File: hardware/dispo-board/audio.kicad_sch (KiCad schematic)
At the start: 41 parts, among them U3 OPA1671, U4 CS5343-CZZ, U5 OPA1671, U6 CS4344-CZZR

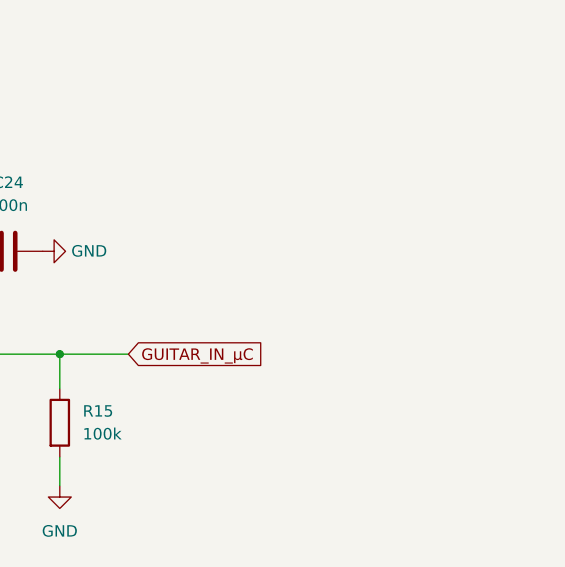
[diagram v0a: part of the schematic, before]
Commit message: basic software, bandpass fir filter, added notes to hardware modifications
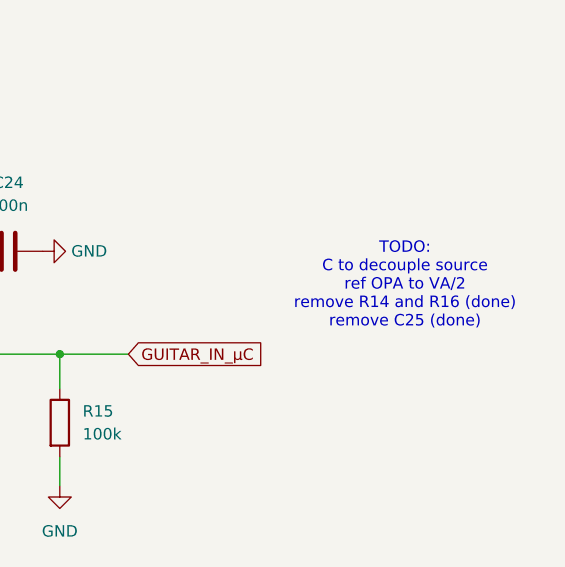
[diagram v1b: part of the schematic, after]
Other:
- note added: "TODO: C to decouple source ref OPA to VA/2 remove R14 and R16 (done) remove C25 (done)"
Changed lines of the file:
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@@
+		)
+	)
+	(text "TODO:\nC to decouple source\nref OPA to VA/2\nremove R14 and R16 (done)\nremove C25 (done)"
+		(exclude_from_sim no)
+		(at 230.124 43.18 0)
+		(effects
+			(font
+				(size 1.27 1.27)
+			)
 		)
 	)

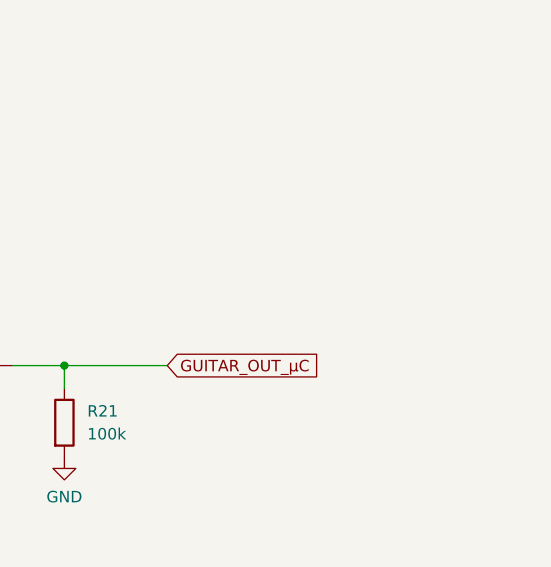
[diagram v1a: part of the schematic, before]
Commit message: audio nucleo changes, kicad notes for hardware issues
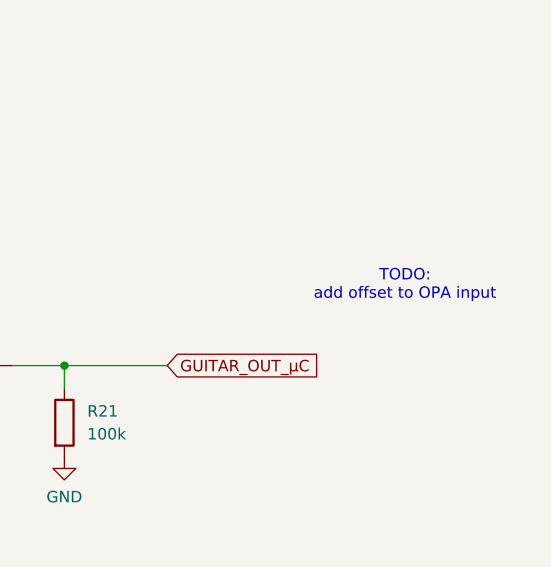
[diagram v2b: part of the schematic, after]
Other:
- note added: "TODO: add offset to OPA input"
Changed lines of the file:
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@@
+		)
+	)
+	(text "TODO:\nadd offset to OPA input"
+		(exclude_from_sim no)
+		(at 241.046 123.19 0)
+		(effects
+			(font
+				(size 1.27 1.27)
+			)
 		)
 	)

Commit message: abgabe version
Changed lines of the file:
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@@
 	(text "TODO:\nC to decouple source\nref OPA to VA/2\nremove R14 and R16 (done)\nremove C25 (done)"
 		(exclude_from_sim no)
-		(at 230.124 43.18 0)
+		(at 316.992 46.99 0)
 		(effects
 			(font
@@
 	(text "TODO:\nadd offset to OPA input"
 		(exclude_from_sim no)
-		(at 241.046 123.19 0)
+		(at 315.468 124.968 0)
 		(effects
 			(font

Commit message: schematic should be ready, changed parts, ...
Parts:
- removed C24, C30, C35: 100n, Capacitor_SMD:C_0402_1005Metric, symbol Device:C
- removed C31: 3u3, Capacitor_SMD:C_0603_1608Metric, symbol Device:C
- removed C33: 10n, Capacitor_SMD:C_0402_1005Metric, symbol Device:C
- removed C36: 10u, Capacitor_SMD:C_0603_1608Metric, symbol Device:C
- removed R19: 10k, Resistor_SMD:R_0402_1005Metric, symbol Device:R
- removed TP5: TestPoint, TestPoint:TestPoint_Pad_D1.5mm, symbol Connector:TestPoint
- removed U6: CS4344-CZZR, Package_SO:TSSOP-10_3x3mm_P0.5mm, symbol Audio:CS4344
- added C14: 10u, Capacitor_SMD:C_0603_1608Metric, symbol Device:C
- added C41: 10n, Capacitor_SMD:C_0402_1005Metric, symbol Device:C
- added C5, C6, C8: 100n, Capacitor_SMD:C_0402_1005Metric, symbol Device:C
- added U2: CS4344, Package_SO:TSSOP-10_3x3mm_P0.5mm, symbol Audio:CS4344
- C25, C32: value 1u -> 100n; footprint Capacitor_SMD:C_1206_3216Metric -> Capacitor_SMD:C_1210_3225Metric; MOUSER_NR 598-FCA1206A105M-H3 -> 667-ECH-U1C104JX5
- C26: MOUSER_NR 81-GRM1555C1H181JA1J -> 81-GCM1555C1H181JA6D
- C27, C29, C34: MOUSER_NR 81-GRM188C81A106MA3D -> 963-LMK107BBJ106MALT
- C28: MOUSER_NR 81-GRM15R61A104KA01J -> 963-MCASL105SB7104KF
- R13, R16: MOUSER_NR 71-CRCW040210K0FKEDC -> 652-CR0402-JW-103GLF
- R14: value 1k -> 10k; MOUSER_NR 71-CRCW0402-1.0K-E3 -> 71-CRCW040210K0FKEDC; now not fitted; now left out of the parts list
- R15, R21: footprint Resistor_SMD:R_0603_1608Metric -> Resistor_SMD:R_0402_1005Metric; MOUSER_NR 594-MCT0603MG1003BP5 -> 652-CR0402JW-104GLF
- R18: MOUSER_NR 667-ERA-2VEB4700X -> 667-ERA-2VEB4700X
- R22: now not fitted; now left out of the parts list
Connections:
- net +3.3VA: no longer U4.10 (VA)
- net GND: now also C14.2, C41.2, C5.2, C6.2, C8.2, U2.8 (GND)
- net GUITAR_IN_µC: now also C25.2; no longer R15.1, U3.3 (+)
- net I2S6_CK: now also U2.2 (~{DEM}/SCLK)
- net I2S6_MCK: now also U2.4 (MCLK)
- net I2S6_SDO: now also U2.1 (SDIN)
- net I2S6_WS: now also U2.3 (LRCK)
- net at R18.1: now also R14.2, R16.1, TP10.1, U2.10 (AOUTR), U2.7 (AOUTL)
- net at C34.1: now also U2.6 (FILT+)
- net at C26.1, TP4.1, U4.6 (AINL)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: now also RV1.1, U3.1 (OUT); no longer C25.1
- net at C28.1, U4.7 (VQ): now also C14.1; no longer C29.1
- net at R17.2, U5.5 (V+): now also R14.1, C6.1
- net at R12.2, U3.5 (V+): now also C5.1
- net at R18.2, TP11.1, U5.3 (+): now also C41.1
- new net: C25.1, R15.1, U3.3 (+)
- new net: C29.1, C8.1, U2.5 (VQ)
- new net +5VA: U2.9 (VA), U4.10 (VA)
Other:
- note added: "TODO: C to decouple source (done) ref OPA to VA/2 (cs5343 input_max = 0.5 va) remove R14 and R16 (done) remove C25 (done)"
- note added: "TODO: add offset to OPA input and output (propably not required)"
- note removed: "TODO: C to decouple source ref OPA to VA/2 remove R14 and R16 (done) remove C25 (done)"
- note removed: "TODO: add offset to OPA input"
- moved on the sheet: C26, R17, R18, RV1, RV2, TP1, TP10, TP11, TP2, TP3, TP6, TP7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

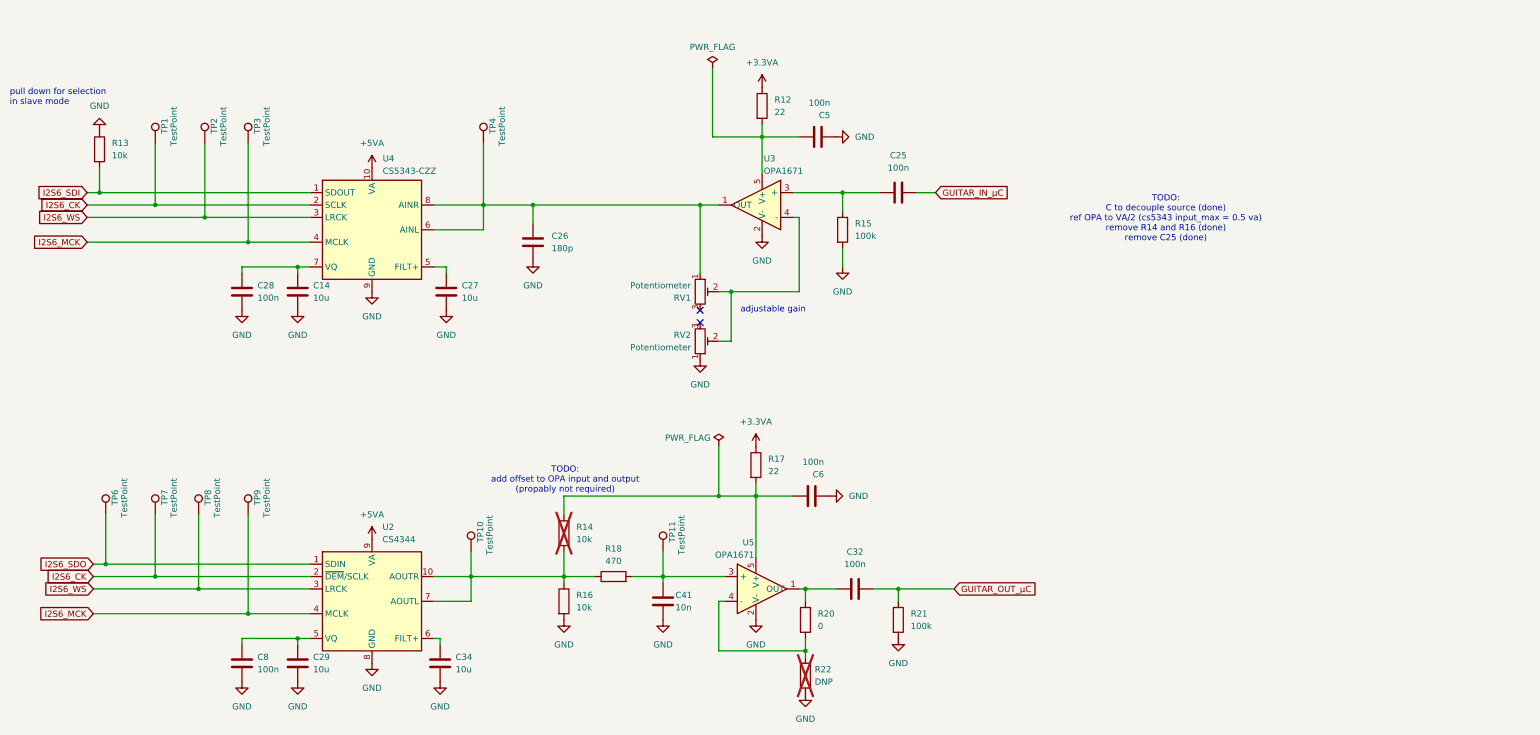
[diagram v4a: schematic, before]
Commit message: deleted nucleo board files, schematic ready?, changed to usb c
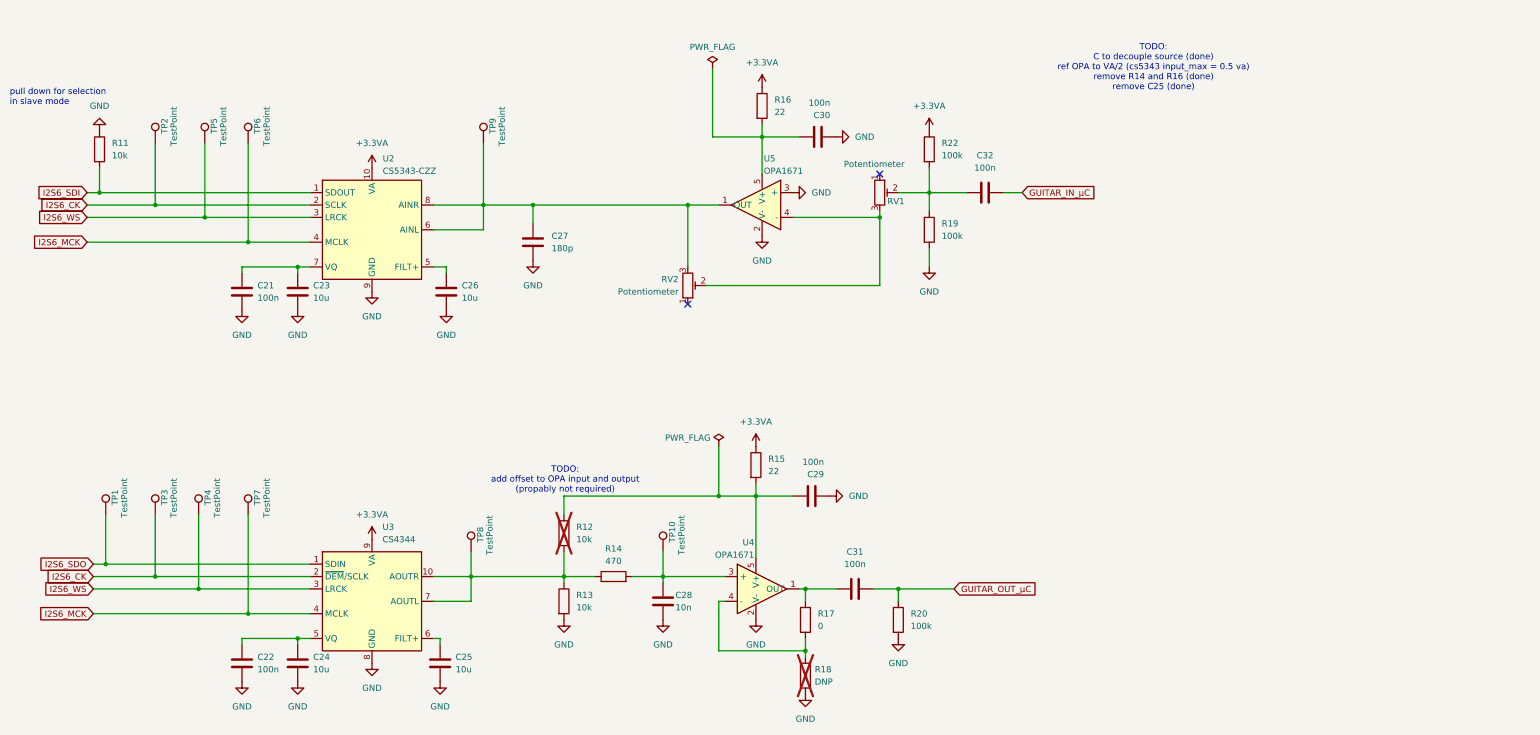
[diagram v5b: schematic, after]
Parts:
- added R22: 100k, Resistor_SMD:R_0402_1005Metric, symbol Device:R
- renumbered C28 to C21, C8 to C22, C14 to C23, C29 to C24, C34 to C25, C27 to C26, C26 to C27, C41 to C28, C6 to C29, C5 to C30, C32 to C31, C25 to C32, R13 to R11, R14 to R12, R16 to R13, R18 to R14, R17 to R15, R12 to R16, R20 to R17, R22 to R18, R15 to R19, R21 to R20, TP6 to TP1, TP11 to TP10, TP1 to TP2, TP7 to TP3, TP8 to TP4, TP2 to TP5, TP3 to TP6, TP9 to TP7, TP10 to TP8, TP4 to TP9, U4 to U2, U2 to U3, U5 to U4, U3 to U5
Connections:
- net +5VA is gone; now on net +3.3VA: U2.10 (VA), U3.9 (VA)
- net +3.3VA: now also R22.1
- net GND: now also U5.3 (+); no longer RV2.1
- net at C32.1, R19.1: now also RV1.2, R22.2; no longer U5.3 (+)
- net at RV2.2, U5.4 (-): now also RV1.3; no longer RV1.2
- net at RV2.3: now also C27.1, TP9.1, U2.6 (AINL), U2.8 (AINR), U5.1 (OUT)
- now unconnected: RV1.1
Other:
- note removed: "adjustable gain"
- moved on the sheet: C32, R19, RV1, RV2

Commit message: annotate schmetic
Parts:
- renumbered R20 to R19, R22 to R20, R19 to R21, RV2 to RV1, RV1 to RV2
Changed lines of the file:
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@@
 		(dnp no)
 		(fields_autoplaced yes)
-		(property "Reference" "#PWR053"
+		(property "Reference" "#PWR054"
 			(at 80.01 81.28 0)
 			(effects
@@
 			(project "dispo-board"
 				(path "/93ea4da8-8485-4fb5-a89d-c72021d94c09/9fac87bb-1399-44df-bfcb-579232522de8"
-					(reference "#PWR053")
+					(reference "#PWR054")
 					(unit 1)
 				)
@@
 		(dnp no)
 		(fields_autoplaced yes)
-		(property "Reference" "#PWR054"
+		(property "Reference" "#PWR055"
 			(at 80.01 157.48 0)
 			(effects
@@
 			(project "dispo-board"
 				(path "/93ea4da8-8485-4fb5-a89d-c72021d94c09/9fac87bb-1399-44df-bfcb-579232522de8"
-					(reference "#PWR054")
+					(reference "#PWR055")
 					(unit 1)
 				)
@@
 		(dnp no)
 		(fields_autoplaced yes)
-		(property "Reference" "R19"
+		(property "Reference" "R21"
 			(at 212.09 57.15 0)
 			(effects
@@
 			(project "dispo-board"
 				(path "/93ea4da8-8485-4fb5-a89d-c72021d94c09/9fac87bb-1399-44df-bfcb-579232522de8"
-					(reference "R19")
+					(reference "R21")
 					(unit 1)
 				)
@@
 		(dnp no)
 		(fields_autoplaced yes)
-		(property "Reference" "#PWR063"
+		(property "Reference" "#PWR064"
 			(at 154.94 144.78 0)
 			(effects
@@
 			(project "dispo-board"
 				(path "/93ea4da8-8485-4fb5-a89d-c72021d94c09/9fac87bb-1399-44df-bfcb-579232522de8"
-					(reference "#PWR063")
+					(reference "#PWR064")
 					(unit 1)
 				)
@@
 		(on_board yes)
 		(dnp no)
-		(property "Reference" "RV2"
+		(property "Reference" "RV1"
 			(at 158.115 68.58 0)
 			(effects
@@
 			(project "dispo-board"
 				(path "/93ea4da8-8485-4fb5-a89d-c72021d94c09/9fac87bb-1399-44df-bfcb-579232522de8"
-					(reference "RV2")
+					(reference "RV1")
 					(unit 1)
 				)
@@
 		(dnp no)
 		(fields_autoplaced yes)
-		(property "Reference" "#PWR052"
+		(property "Reference" "#PWR053"
 			(at 68.58 157.48 0)
 			(effects
@@
 			(project "dispo-board"
 				(path "/93ea4da8-8485-4fb5-a89d-c72021d94c09/9fac87bb-1399-44df-bfcb-579232522de8"
-					(reference "#PWR052")
+					(reference "#PWR053")
 					(unit 1)
 				)
@@
 		(dnp no)
 		(fields_autoplaced yes)
-		(property "Reference" "#PWR056"
+		(property "Reference" "#PWR057"
 			(at 95.25 77.47 0)
 			(effects
@@
 			(project "dispo-board"
 				(path "/93ea4da8-8485-4fb5-a89d-c72021d94c09/9fac87bb-1399-44df-bfcb-579232522de8"
-					(reference "#PWR056")
+					(reference "#PWR057")
 					(unit 1)
 				)
@@
 		(dnp no)
 		(fields_autoplaced yes)
-		(property "Reference" "R20"
+		(property "Reference" "R19"
 			(at 205.74 137.16 0)
 			(effects
@@
 			(project "dispo-board"
 				(path "/93ea4da8-8485-4fb5-a89d-c72021d94c09/9fac87bb-1399-44df-bfcb-579232522de8"
-					(reference "R20")
+					(reference "R19")
 					(unit 1)
 				)
@@
 		(dnp no)
 		(fields_autoplaced yes)
-		(property "Reference" "#PWR064"
+		(property "Reference" "#PWR069"
 			(at 187.96 50.8 0)
 			(effects
@@
 			(project ""
 				(path "/93ea4da8-8485-4fb5-a89d-c72021d94c09/9fac87bb-1399-44df-bfcb-579232522de8"
-					(reference "#PWR064")
+					(reference "#PWR069")
 					(unit 1)
 				)
@@
 		(dnp no)
 		(fields_autoplaced yes)
-		(property "Reference" "#PWR051"
+		(property "Reference" "#PWR052"
 			(at 68.58 81.28 0)
 			(effects
@@
 			(project ""
 				(path "/93ea4da8-8485-4fb5-a89d-c72021d94c09/9fac87bb-1399-44df-bfcb-579232522de8"
-					(reference "#PWR051")
+					(reference "#PWR052")
 					(unit 1)
 				)
@@
 		(dnp no)
 		(fields_autoplaced yes)
-		(property "Reference" "#PWR070"
+		(property "Reference" "#PWR071"
 			(at 195.58 113.03 0)
 			(effects
@@
 			(project "dispo-board"
 				(path "/93ea4da8-8485-4fb5-a89d-c72021d94c09/9fac87bb-1399-44df-bfcb-579232522de8"
-					(reference "#PWR070")
+					(reference "#PWR071")
 					(unit 1)
 				)
@@
 		(dnp no)
 		(fields_autoplaced yes)
-		(property "Reference" "#PWR062"
+		(property "Reference" "#PWR063"
 			(at 134.62 144.78 0)
 			(effects
@@
 			(project "dispo-board"
 				(path "/93ea4da8-8485-4fb5-a89d-c72021d94c09/9fac87bb-1399-44df-bfcb-579232522de8"
-					(reference "#PWR062")
+					(reference "#PWR063")
 					(unit 1)
 				)
@@
 		(dnp no)
 		(fields_autoplaced yes)
-		(property "Reference" "#PWR059"
+		(property "Reference" "#PWR060"
 			(at 109.22 157.48 0)
 			(effects
@@
 			(project "dispo-board"
 				(path "/93ea4da8-8485-4fb5-a89d-c72021d94c09/9fac87bb-1399-44df-bfcb-579232522de8"
-					(reference "#PWR059")
+					(reference "#PWR060")
 					(unit 1)
 				)
@@
 		(dnp no)
 		(fields_autoplaced yes)
-		(property "Reference" "#PWR071"
+		(property "Reference" "#PWR072"
 			(at 196.85 39.37 0)
 			(effects
@@
 			(project "dispo-board"
 				(path "/93ea4da8-8485-4fb5-a89d-c72021d94c09/9fac87bb-1399-44df-bfcb-579232522de8"
-					(reference "#PWR071")
+					(reference "#PWR072")
 					(unit 1)
 				)
@@
 		(dnp no)
 		(fields_autoplaced yes)
-		(property "Reference" "#PWR057"
+		(property "Reference" "#PWR056"
 			(at 95.25 49.53 0)
 			(effects
@@
 			(project "dispo-board"
 				(path "/93ea4da8-8485-4fb5-a89d-c72021d94c09/9fac87bb-1399-44df-bfcb-579232522de8"
-					(reference "#PWR057")
+					(reference "#PWR056")
 					(unit 1)
 				)
@@
 		(dnp no)
 		(fields_autoplaced yes)
-		(property "Reference" "#PWR091"
+		(property "Reference" "#PWR074"
 			(at 209.55 41.91 0)
 			(effects
@@
 			(project "dispo-board"
 				(path "/93ea4da8-8485-4fb5-a89d-c72021d94c09/9fac87bb-1399-44df-bfcb-579232522de8"
-					(reference "#PWR091")
+					(reference "#PWR074")
 					(unit 1)
 				)
@@
 		(dnp no)
 		(fields_autoplaced yes)
-		(property "Reference" "#PWR060"
+		(property "Reference" "#PWR061"
 			(at 110.49 81.28 0)
 			(effects
@@
 			(project "dispo-board"
 				(path "/93ea4da8-8485-4fb5-a89d-c72021d94c09/9fac87bb-1399-44df-bfcb-579232522de8"
-					(reference "#PWR060")
+					(reference "#PWR061")
 					(unit 1)
 				)
@@
 		(on_board yes)
 		(dnp no)
-		(property "Reference" "RV1"
+		(property "Reference" "RV2"
 			(at 204.47 52.578 0)
 			(effects
@@
 			(project "dispo-board"
 				(path "/93ea4da8-8485-4fb5-a89d-c72021d94c09/9fac87bb-1399-44df-bfcb-579232522de8"
-					(reference "RV1")
+					(reference "RV2")
 					(unit 1)
 				)
@@
 		(dnp no)
 		(fields_autoplaced yes)
-		(property "Reference" "#PWR055"
+		(property "Reference" "#PWR058"
 			(at 95.25 125.73 0)
 			(effects
@@
 			(project "dispo-board"
 				(path "/93ea4da8-8485-4fb5-a89d-c72021d94c09/9fac87bb-1399-44df-bfcb-579232522de8"
-					(reference "#PWR055")
+					(reference "#PWR058")
 					(unit 1)
 				)
@@
 		(dnp no)
 		(fields_autoplaced yes)
-		(property "Reference" "#PWR058"
+		(property "Reference" "#PWR059"
 			(at 95.25 153.67 0)
 			(effects
@@
 			(project "dispo-board"
 				(path "/93ea4da8-8485-4fb5-a89d-c72021d94c09/9fac87bb-1399-44df-bfcb-579232522de8"
-					(reference "#PWR058")
+					(reference "#PWR059")
 					(unit 1)
 				)
@@
 		(dnp no)
 		(fields_autoplaced yes)
-		(property "Reference" "#PWR072"
+		(property "Reference" "#PWR075"
 			(at 209.55 72.39 0)
 			(effects
@@
 			(project "dispo-board"
 				(path "/93ea4da8-8485-4fb5-a89d-c72021d94c09/9fac87bb-1399-44df-bfcb-579232522de8"
-					(reference "#PWR072")
+					(reference "#PWR075")
 					(unit 1)
 				)
@@
 		(dnp no)
 		(fields_autoplaced yes)
-		(property "Reference" "R22"
+		(property "Reference" "R20"
 			(at 212.09 40.64 0)
 			(effects
@@
 			(project "dispo-board"
 				(path "/93ea4da8-8485-4fb5-a89d-c72021d94c09/9fac87bb-1399-44df-bfcb-579232522de8"
-					(reference "R22")
+					(reference "R20")
 					(unit 1)
 				)
@@
 		(dnp no)
 		(fields_autoplaced yes)
-		(property "Reference" "#PWR050"
+		(property "Reference" "#PWR051"
 			(at 39.37 31.75 0)
 			(effects
@@
 			(project ""
 				(path "/93ea4da8-8485-4fb5-a89d-c72021d94c09/9fac87bb-1399-44df-bfcb-579232522de8"
-					(reference "#PWR050")
+					(reference "#PWR051")
 					(unit 1)
 				)
@@
 		(dnp no)
 		(fields_autoplaced yes)
-		(property "Reference" "#PWR061"
+		(property "Reference" "#PWR062"
 			(at 128.27 71.12 0)
 			(effects
@@
 			(project "dispo-board"
 				(path "/93ea4da8-8485-4fb5-a89d-c72021d94c09/9fac87bb-1399-44df-bfcb-579232522de8"
-					(reference "#PWR061")
+					(reference "#PWR062")
 					(unit 1)
 				)
@@
 		(dnp no)
 		(fields_autoplaced yes)
-		(property "Reference" "#PWR069"
+		(property "Reference" "#PWR070"
 			(at 184.15 160.02 0)
 			(effects
@@
 			(project "dispo-board"
 				(path "/93ea4da8-8485-4fb5-a89d-c72021d94c09/9fac87bb-1399-44df-bfcb-579232522de8"
-					(reference "#PWR069")
+					(reference "#PWR070")
 					(unit 1)
 				)

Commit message: shorted board
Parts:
- R12: now fitted; now in the parts list
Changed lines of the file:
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@@
 		(unit 1)
 		(exclude_from_sim no)
-		(in_bom no)
+		(in_bom yes)
 		(on_board yes)
-		(dnp yes)
+		(dnp no)
 		(fields_autoplaced yes)
 		(property "Reference" "R12"

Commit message: routing almost finished, need GND plane
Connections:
- net I2S6_CK: no longer TP2.1
- net I2S6_SDI: now also TP2.1
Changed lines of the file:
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@@
+	)
+	(junction
+		(at 50.8 50.8)
+		(diameter 0)
+		(color 0 0 0 0)
 	)
 	(junction
 		(at 203.2 132.08)
-		(diameter 0)
-		(color 0 0 0 0)
-	)
-	(junction
-		(at 50.8 53.34)
 		(diameter 0)
 		(color 0 0 0 0)
@@
 	(wire
 		(pts
+			(xy 50.8 40.64) (xy 50.8 50.8)
+		)
+		(stroke
+			(width 0)
+			(type default)
+		)
+	)
+	(wire
+		(pts
 			(xy 107.95 142.24) (xy 109.22 142.24)
 		)
@@
 	(wire
 		(pts
-			(xy 39.37 50.8) (xy 82.55 50.8)
+			(xy 39.37 50.8) (xy 50.8 50.8)
 		)
 		(stroke
@@
 	(wire
 		(pts
-			(xy 36.83 53.34) (xy 50.8 53.34)
-		)
-		(stroke
-			(width 0)
-			(type default)
-		)
-	)
-	(wire
-		(pts
 			(xy 68.58 142.24) (xy 80.01 142.24)
 		)
@@
 	(wire
 		(pts
-			(xy 50.8 53.34) (xy 82.55 53.34)
+			(xy 36.83 53.34) (xy 82.55 53.34)
 		)
 		(stroke
@@
 	(wire
 		(pts
+			(xy 50.8 50.8) (xy 82.55 50.8)
+		)
+		(stroke
+			(width 0)
+			(type default)
+		)
+	)
+	(wire
+		(pts
 			(xy 69.85 116.84) (xy 69.85 137.16)
 		)
@@
 		)
 		(stroke
-			(width 0)
-			(type default)
-		)
-	)
-	(wire
-		(pts
-			(xy 50.8 40.64) (xy 50.8 53.34)
-		)
-		(stroke
